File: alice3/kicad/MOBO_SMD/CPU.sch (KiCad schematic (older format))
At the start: 5 parts, among them U1 Z80CPU-SMD, U6 AS6C2008_TSOP

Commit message: Assign parts to footprints.
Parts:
- U1: footprint (none) -> Housings_QFP:LQFP-44_10x10mm_Pitch0.8mm
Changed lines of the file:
@@
 $EndDescr
 $Comp
-L GND #PWR42
+L GND #PWR042
 U 1 1 568DE0B3
 P 3950 4600
-F 0 "#PWR42" H 3950 4350 50  0001 C CNN
+F 0 "#PWR042" H 3950 4350 50  0001 C CNN
 F 1 "GND" H 3950 4450 50  0000 C CNN
 F 2 "" H 3950 4600 50  0000 C CNN
@@
 /Z80_RESET
 $Comp
-L GND #PWR40
+L GND #PWR043
 U 1 1 568DF463
 P 2200 2600
-F 0 "#PWR40" H 2200 2350 50  0001 C CNN
+F 0 "#PWR043" H 2200 2350 50  0001 C CNN
 F 1 "GND" H 2200 2450 50  0000 C CNN
 F 2 "" H 2200 2600 50  0000 C CNN
@@
 	3300 3100 3400 3100
 $Comp
-L GND #PWR44
+L GND #PWR044
 U 1 1 56A06CAB
 P 4450 1200
-F 0 "#PWR44" H 4450 950 50  0001 C CNN
+F 0 "#PWR044" H 4450 950 50  0001 C CNN
 F 1 "GND" H 4450 1050 50  0000 C CNN
 F 2 "" H 4450 1200 50  0000 C CNN
@@
 $EndComp
 $Comp
-L GND #PWR48
+L GND #PWR045
 U 1 1 56A06F73
 P 8100 1500
-F 0 "#PWR48" H 8100 1250 50  0001 C CNN
+F 0 "#PWR045" H 8100 1250 50  0001 C CNN
 F 1 "GND" H 8100 1350 50  0000 C CNN
 F 2 "" H 8100 1500 50  0000 C CNN
@@
 $EndComp
 $Comp
-L +3V3 #PWR43
+L +3V3 #PWR046
 U 1 1 56A5493F
 P 4100 800
-F 0 "#PWR43" H 4100 650 50  0001 C CNN
+F 0 "#PWR046" H 4100 650 50  0001 C CNN
 F 1 "+3V3" H 4100 940 50  0000 C CNN
 F 2 "" H 4100 800 60  0000 C CNN
@@
 $EndComp
 $Comp
-L +3V3 #PWR41
+L +3V3 #PWR047
 U 1 1 56A55184
 P 3200 2350
-F 0 "#PWR41" H 3200 2200 50  0001 C CNN
+F 0 "#PWR047" H 3200 2200 50  0001 C CNN
 F 1 "+3V3" H 3200 2490 50  0000 C CNN
 F 2 "" H 3200 2350 60  0000 C CNN
@@
 D0
 $Comp
-L GND #PWR47
+L GND #PWR048
 U 1 1 56CACCBC
 P 7650 4375
-F 0 "#PWR47" H 7650 4125 50  0001 C CNN
+F 0 "#PWR048" H 7650 4125 50  0001 C CNN
 F 1 "GND" H 7650 4225 50  0000 C CNN
 F 2 "" H 7650 4375 50  0000 C CNN
@@
 $EndComp
 $Comp
-L +3V3 #PWR46
+L +3V3 #PWR049
 U 1 1 56CACE05
 P 7650 900
-F 0 "#PWR46" H 7650 750 50  0001 C CNN
+F 0 "#PWR049" H 7650 750 50  0001 C CNN
 F 1 "+3V3" H 7650 1040 50  0000 C CNN
 F 2 "" H 7650 900 60  0000 C CNN
@@
 $EndComp
 $Comp
-L GND #PWR45
+L GND #PWR050
 U 1 1 56CACF44
 P 6400 3875
-F 0 "#PWR45" H 6400 3625 50  0001 C CNN
+F 0 "#PWR050" H 6400 3625 50  0001 C CNN
 F 1 "GND" H 6400 3725 50  0000 C CNN
 F 2 "" H 6400 3875 50  0000 C CNN
@@
 F 0 "U1" H 3550 4400 50  0000 L CNN
 F 1 "Z80CPU-SMD" H 4200 4400 50  0000 L CNN
-F 2 "" H 4100 3400 50  0000 C CNN
+F 2 "Housings_QFP:LQFP-44_10x10mm_Pitch0.8mm" H 4100 3400 50  0001 C CNN
 F 3 "" H 4100 3400 50  0000 C CNN
 	1    4100 3000
@@
 F 0 "U6" H 7425 4125 50  0000 C CNN
 F 1 "AS6C2008_TSOP" H 8025 1600 50  0000 C CNN
-F 2 "" H 7750 2925 50  0000 C CNN
+F 2 "" H 7750 2925 50  0001 C CNN
 F 3 "" H 7750 2925 50  0000 C CNN
 	1    7750 2925

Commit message: Fix some footprint assignments.
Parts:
- U6: footprint (none) -> SMD_Packages:TSOP32SP
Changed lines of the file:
@@
 $EndDescr
 $Comp
-L GND #PWR042
+L GND #PWR043
 U 1 1 568DE0B3
 P 3950 4600
-F 0 "#PWR042" H 3950 4350 50  0001 C CNN
+F 0 "#PWR043" H 3950 4350 50  0001 C CNN
 F 1 "GND" H 3950 4450 50  0000 C CNN
 F 2 "" H 3950 4600 50  0000 C CNN
@@
 /Z80_RESET
 $Comp
-L GND #PWR043
+L GND #PWR044
 U 1 1 568DF463
 P 2200 2600
-F 0 "#PWR043" H 2200 2350 50  0001 C CNN
+F 0 "#PWR044" H 2200 2350 50  0001 C CNN
 F 1 "GND" H 2200 2450 50  0000 C CNN
 F 2 "" H 2200 2600 50  0000 C CNN
@@
 	3300 3100 3400 3100
 $Comp
-L GND #PWR044
+L GND #PWR045
 U 1 1 56A06CAB
 P 4450 1200
-F 0 "#PWR044" H 4450 950 50  0001 C CNN
+F 0 "#PWR045" H 4450 950 50  0001 C CNN
 F 1 "GND" H 4450 1050 50  0000 C CNN
 F 2 "" H 4450 1200 50  0000 C CNN
@@
 $EndComp
 $Comp
-L GND #PWR045
+L GND #PWR046
 U 1 1 56A06F73
 P 8100 1500
-F 0 "#PWR045" H 8100 1250 50  0001 C CNN
+F 0 "#PWR046" H 8100 1250 50  0001 C CNN
 F 1 "GND" H 8100 1350 50  0000 C CNN
 F 2 "" H 8100 1500 50  0000 C CNN
@@
 $EndComp
 $Comp
-L +3V3 #PWR046
+L +3V3 #PWR047
 U 1 1 56A5493F
 P 4100 800
-F 0 "#PWR046" H 4100 650 50  0001 C CNN
+F 0 "#PWR047" H 4100 650 50  0001 C CNN
 F 1 "+3V3" H 4100 940 50  0000 C CNN
 F 2 "" H 4100 800 60  0000 C CNN
@@
 $EndComp
 $Comp
-L +3V3 #PWR047
+L +3V3 #PWR048
 U 1 1 56A55184
 P 3200 2350
-F 0 "#PWR047" H 3200 2200 50  0001 C CNN
+F 0 "#PWR048" H 3200 2200 50  0001 C CNN
 F 1 "+3V3" H 3200 2490 50  0000 C CNN
 F 2 "" H 3200 2350 60  0000 C CNN
@@
 D0
 $Comp
-L GND #PWR048
+L GND #PWR049
 U 1 1 56CACCBC
 P 7650 4375
-F 0 "#PWR048" H 7650 4125 50  0001 C CNN
+F 0 "#PWR049" H 7650 4125 50  0001 C CNN
 F 1 "GND" H 7650 4225 50  0000 C CNN
 F 2 "" H 7650 4375 50  0000 C CNN
@@
 $EndComp
 $Comp
-L +3V3 #PWR049
+L +3V3 #PWR050
 U 1 1 56CACE05
 P 7650 900
-F 0 "#PWR049" H 7650 750 50  0001 C CNN
+F 0 "#PWR050" H 7650 750 50  0001 C CNN
 F 1 "+3V3" H 7650 1040 50  0000 C CNN
 F 2 "" H 7650 900 60  0000 C CNN
@@
 $EndComp
 $Comp
-L GND #PWR050
+L GND #PWR051
 U 1 1 56CACF44
 P 6400 3875
-F 0 "#PWR050" H 6400 3625 50  0001 C CNN
+F 0 "#PWR051" H 6400 3625 50  0001 C CNN
 F 1 "GND" H 6400 3725 50  0000 C CNN
 F 2 "" H 6400 3875 50  0000 C CNN
@@
 F 0 "U6" H 7425 4125 50  0000 C CNN
 F 1 "AS6C2008_TSOP" H 8025 1600 50  0000 C CNN
-F 2 "" H 7750 2925 50  0001 C CNN
+F 2 "SMD_Packages:TSOP32SP" H 7750 2925 50  0001 C CNN
 F 3 "" H 7750 2925 50  0000 C CNN
 	1    7750 2925

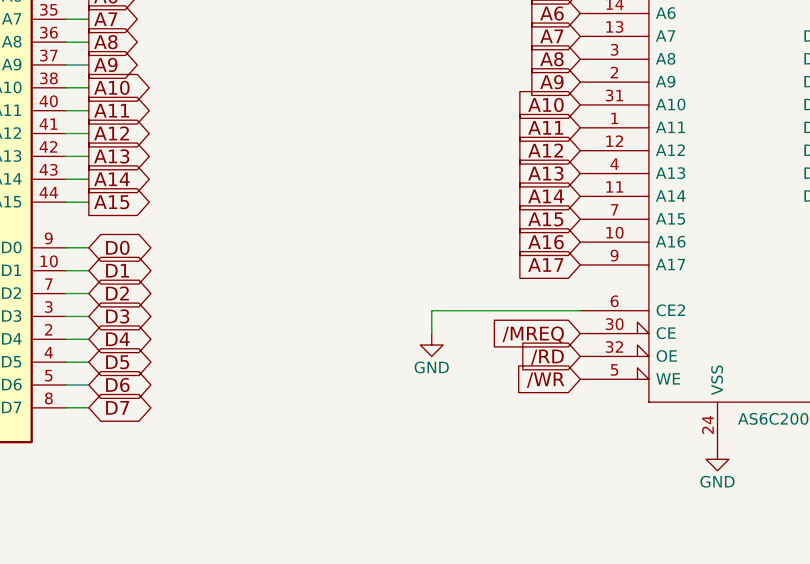
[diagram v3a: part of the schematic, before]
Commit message: Point out bug in Alice 3 schematic.
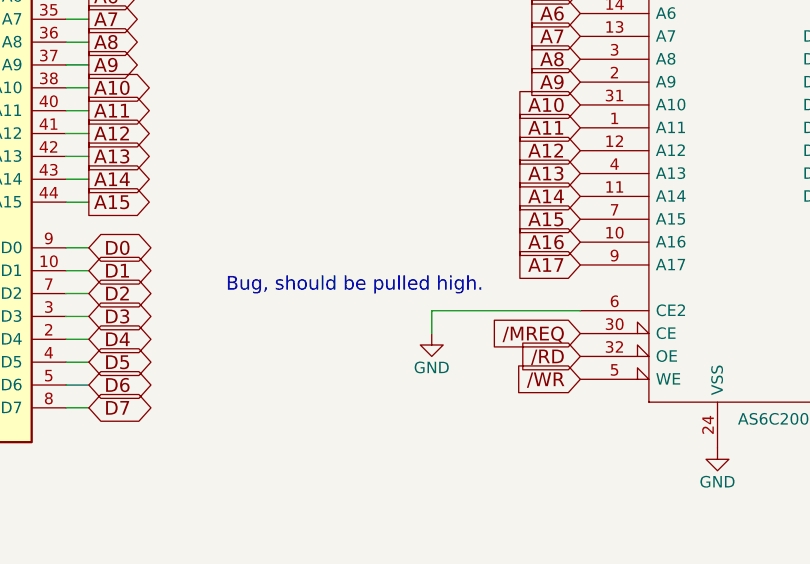
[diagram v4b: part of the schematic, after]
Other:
- note added: "Bug, should be pulled high."
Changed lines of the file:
@@
 Wire Wire Line
 	8100 1500 8100 1450
+Text Notes 5500 3700 0    60   ~ 0
+Bug, should be pulled high.
 $EndSCHEMATC

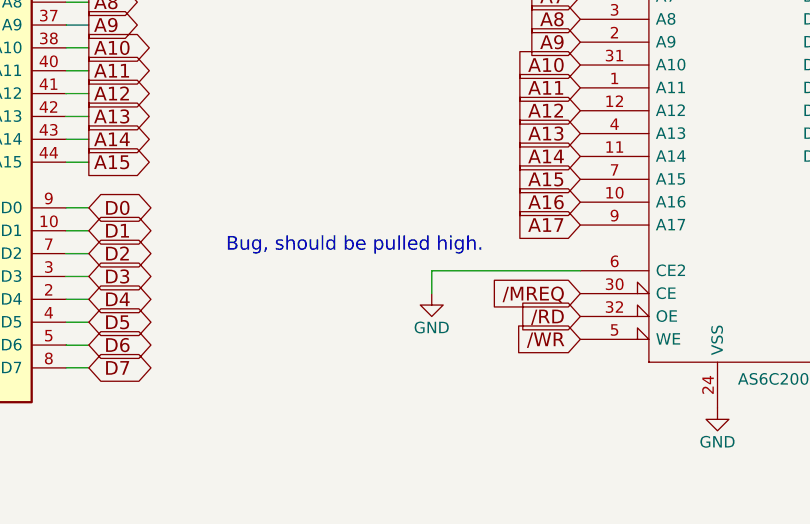
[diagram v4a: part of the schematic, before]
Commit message: make CE2 high
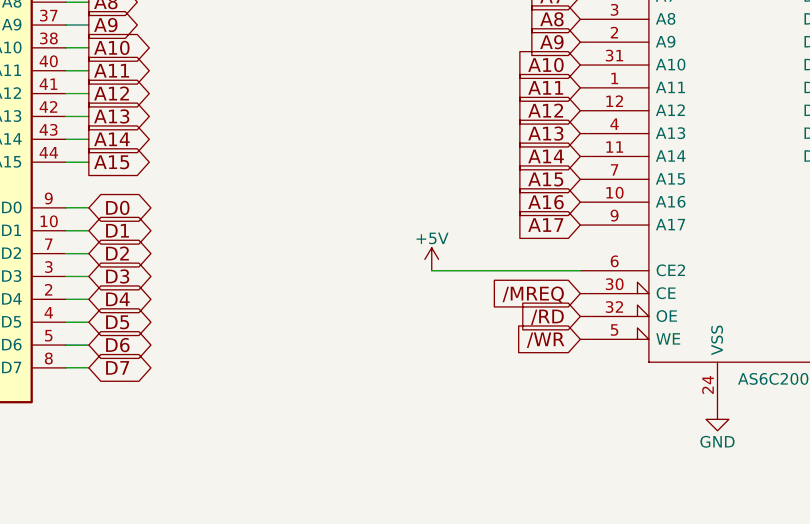
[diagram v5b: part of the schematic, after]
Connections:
- net GND: no longer U6.6 (CE2)
- new net +5V: U6.6 (CE2)
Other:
- note removed: "Bug, should be pulled high."
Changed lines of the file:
@@
-$EndComp
-$Comp
-L GND #PWR050
-U 1 1 56CACF44
-P 6400 3875
-F 0 "#PWR050" H 6400 3625 50  0001 C CNN
-F 1 "GND" H 6400 3725 50  0000 C CNN
-F 2 "" H 6400 3875 50  0000 C CNN
-F 3 "" H 6400 3875 50  0000 C CNN
-	1    6400 3875
-	1    0    0    -1
 $EndComp
 $Comp
@@
 Wire Wire Line
 	7050 3775 6400 3775
-Wire Wire Line
-	6400 3775 6400 3875
 Text GLabel 7050 3575 0    60   Input ~ 0
 A17
@@
 Wire Wire Line
 	8100 1500 8100 1450
-Text Notes 5500 3700 0    60   ~ 0
-Bug, should be pulled high.
+$Comp
+L +5V #PWR?
+U 1 1 59948058
+P 6400 3775
+F 0 "#PWR?" H 6400 3625 50  0001 C CNN
+F 1 "+5V" H 6400 3915 50  0000 C CNN
+F 2 "" H 6400 3775 50  0001 C CNN
+F 3 "" H 6400 3775 50  0001 C CNN
+	1    6400 3775
+	1    0    0    -1
+$EndComp
 $EndSCHEMATC

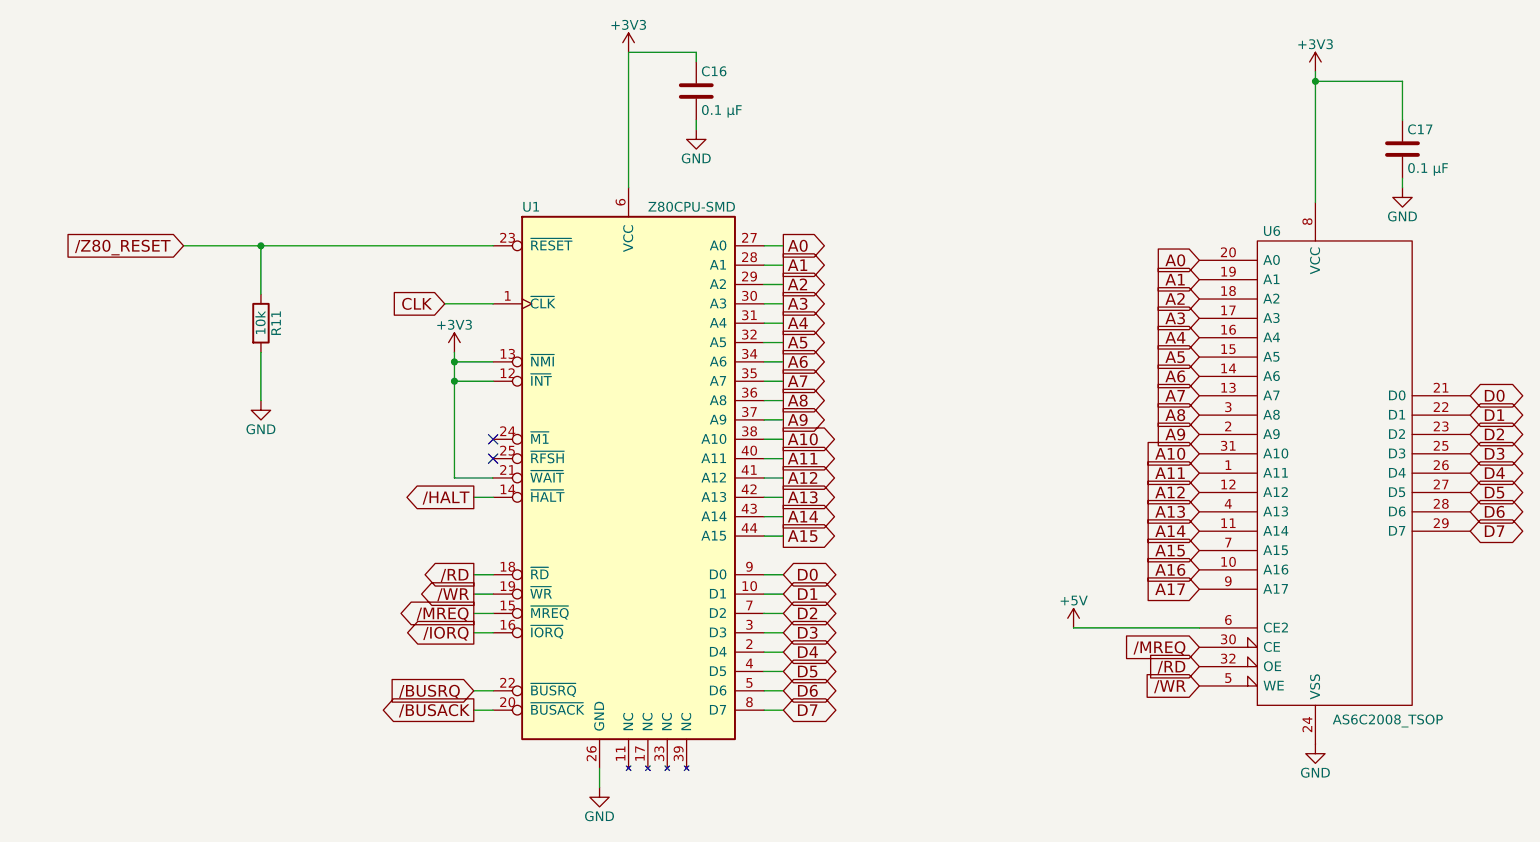
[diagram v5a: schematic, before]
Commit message: 1st set MOBO schematic fixes for 1st PCBWay spin
Various fixes for KiCAD messing up components

Button on BOOT0

No huge cap on power supply LED

Discard RAM

Route ARM to Z80 /WAIT and /RFSH

Use "~" for active-low lines (shown in schematic by line above them)
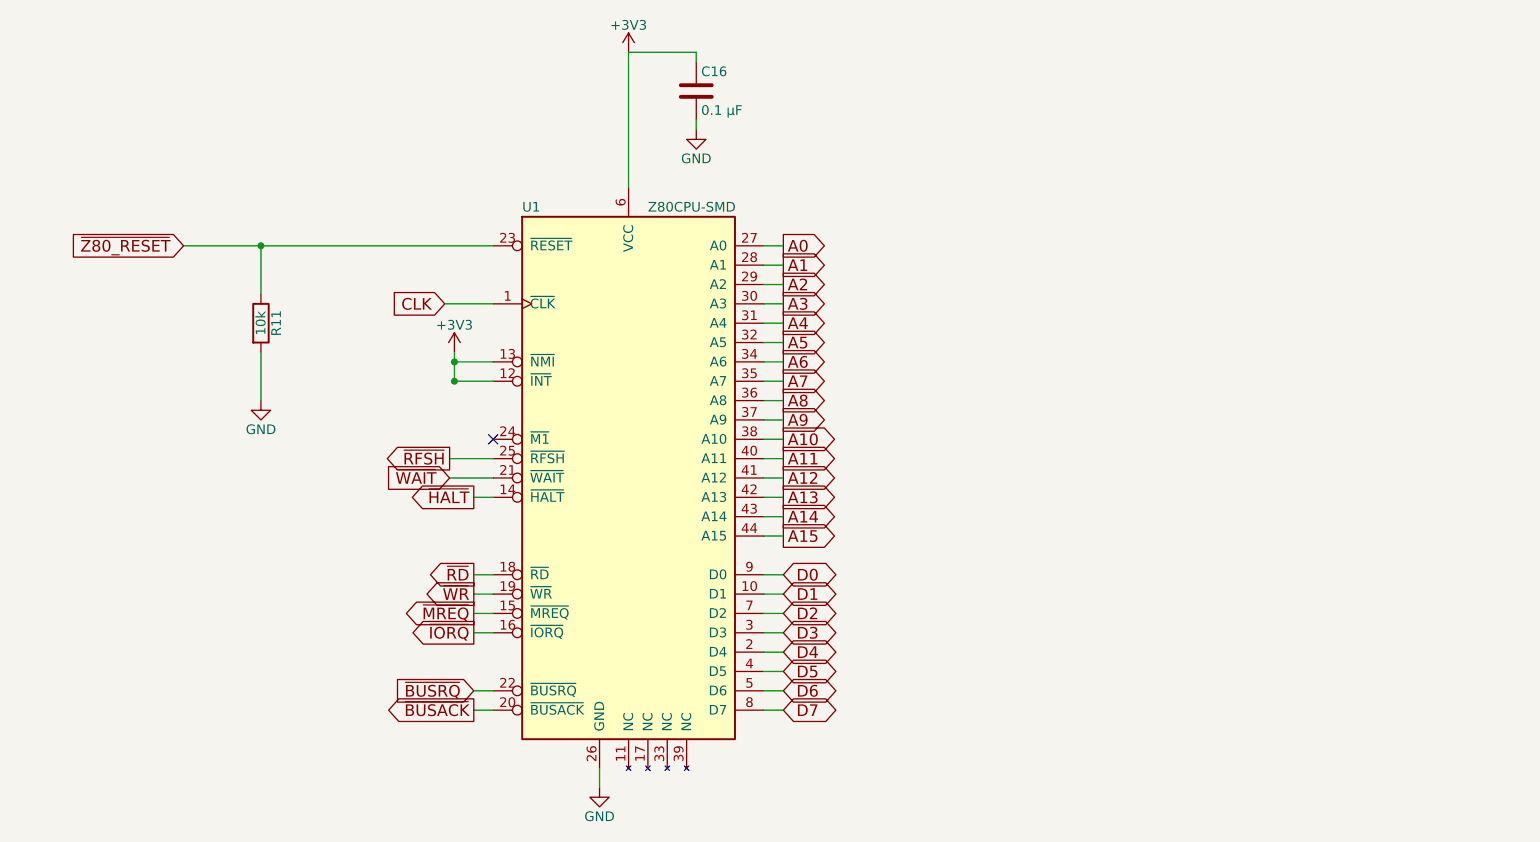
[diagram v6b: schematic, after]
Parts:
- removed C17: 0.1 µF, Capacitors_SMD:C_0805, symbol C
- removed U6: AS6C2008_TSOP, SMD_Packages:TSOP32SP, symbol AS6C2008_TSOP
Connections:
- net +3V3: no longer U1.21 (~WAIT~)
- net ~RFSH: now reaches U1.25 (~RFSH~)
- net /BUSACK renamed ~BUSACK
- net /BUSRQ renamed ~BUSRQ
- net /HALT renamed ~HALT
- net /IORQ renamed ~IORQ
- net /MREQ renamed ~MREQ
- net /RD renamed ~RD
- net /WR renamed ~WR
- net /Z80_RESET renamed ~Z80_RESET
- new net ~WAIT: U1.21 (~WAIT~)
- no-connect marks 2 -> 1
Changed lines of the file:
@@
 $EndDescr
 $Comp
-L GND #PWR042
+L GND #PWR037
 U 1 1 568DE0B3
 P 3950 4600
-F 0 "#PWR042" H 3950 4350 50  0001 C CNN
+F 0 "#PWR037" H 3950 4350 50  0001 C CNN
 F 1 "GND" H 3950 4450 50  0000 C CNN
 F 2 "" H 3950 4600 50  0000 C CNN
@@
 D0
 Wire Wire Line
-	3200 2350 3200 3000
-Wire Wire Line
 	3200 2400 3400 2400
 Connection ~ 3200 2400
 Text GLabel 3300 3500 0    60   Output ~ 0
-/RD
+~RD
 Text GLabel 3300 3600 0    60   Output ~ 0
-/WR
+~WR
 Text GLabel 3300 3700 0    60   Output ~ 0
-/MREQ
+~MREQ
 Text GLabel 3300 3800 0    60   Output ~ 0
-/IORQ
+~IORQ
 Wire Wire Line
 	3300 3500 3400 3500
@@
 Wire Wire Line
 	3300 3800 3400 3800
-NoConn ~ 3400 2900
-Wire Wire Line
-	3200 3000 3400 3000
 NoConn ~ 3400 2800
 Text GLabel 3300 4100 0    60   Input ~ 0
-/BUSRQ
+~BUSRQ
 Text GLabel 3300 4200 0    60   Output ~ 0
-/BUSACK
+~BUSACK
 Wire Wire Line
 	3300 4200 3400 4200
 Text GLabel 1800 1800 0    60   Input ~ 0
-/Z80_RESET
-$Comp
-L GND #PWR043
+~Z80_RESET
+$Comp
+L GND #PWR038
 U 1 1 568DF463
 P 2200 2600
-F 0 "#PWR043" H 2200 2350 50  0001 C CNN
+F 0 "#PWR038" H 2200 2350 50  0001 C CNN
 F 1 "GND" H 2200 2450 50  0000 C CNN
 F 2 "" H 2200 2600 50  0000 C CNN
@@
 Connection ~ 3200 2500
 Text GLabel 3300 3100 0    60   Output ~ 0
-/HALT
+~HALT
 Wire Wire Line
 	3300 3100 3400 3100
 $Comp
-L GND #PWR044
+L GND #PWR039
 U 1 1 56A06CAB
 P 4450 1200
-F 0 "#PWR044" H 4450 950 50  0001 C CNN
+F 0 "#PWR039" H 4450 950 50  0001 C CNN
 F 1 "GND" H 4450 1050 50  0000 C CNN
 F 2 "" H 4450 1200 50  0000 C CNN
@@
 	4450 800  4450 850
 $Comp
-L C C17
-U 1 1 56A06F35
-P 8100 1300
-F 0 "C17" H 8125 1400 50  0000 L CNN
-F 1 "0.1 µF" H 8125 1200 50  0000 L CNN
-F 2 "Capacitors_SMD:C_0805" H 8138 1150 50  0001 C CNN
-F 3 "" H 8100 1300 50  0000 C CNN
-	1    8100 1300
-	1    0    0    -1
-$EndComp
-$Comp
-L GND #PWR045
-U 1 1 56A06F73
-P 8100 1500
-F 0 "#PWR045" H 8100 1250 50  0001 C CNN
-F 1 "GND" H 8100 1350 50  0000 C CNN
-F 2 "" H 8100 1500 50  0000 C CNN
-F 3 "" H 8100 1500 50  0000 C CNN
-	1    8100 1500
-	1    0    0    -1
-$EndComp
-$Comp
-L +3V3 #PWR046
+L +3V3 #PWR040
 U 1 1 56A5493F
 P 4100 800
-F 0 "#PWR046" H 4100 650 50  0001 C CNN
+F 0 "#PWR040" H 4100 650 50  0001 C CNN
 F 1 "+3V3" H 4100 940 50  0000 C CNN
 F 2 "" H 4100 800 60  0000 C CNN
@@
 $EndComp
 $Comp
-L +3V3 #PWR047
+L +3V3 #PWR041
 U 1 1 56A55184
 P 3200 2350
-F 0 "#PWR047" H 3200 2200 50  0001 C CNN
+F 0 "#PWR041" H 3200 2200 50  0001 C CNN
 F 1 "+3V3" H 3200 2490 50  0000 C CNN
 F 2 "" H 3200 2350 60  0000 C CNN
 F 3 "" H 3200 2350 60  0000 C CNN
 	1    3200 2350
-	1    0    0    -1
-$EndComp
-Text GLabel 7050 3375 0    60   Input ~ 0
-A15
-Text GLabel 7050 3275 0    60   Input ~ 0
-A14
-Text GLabel 7050 3175 0    60   Input ~ 0
-A13
-Text GLabel 7050 3075 0    60   Input ~ 0
-A12
-Text GLabel 7050 2975 0    60   Input ~ 0
-A11
-Text GLabel 7050 2875 0    60   Input ~ 0
-A10
-Text GLabel 7050 2775 0    60   Input ~ 0
-A9
-Text GLabel 7050 2675 0    60   Input ~ 0
-A8
-Text GLabel 7050 2575 0    60   Input ~ 0
-A7
-Text GLabel 7050 2475 0    60   Input ~ 0
-A6
-Text GLabel 7050 2375 0    60   Input ~ 0
-A5
-Text GLabel 7050 2275 0    60   Input ~ 0
-A4
-Text GLabel 7050 2175 0    60   Input ~ 0
-A3
-Text GLabel 7050 2075 0    60   Input ~ 0
-A2
-Text GLabel 7050 1975 0    60   Input ~ 0
-A1
-Text GLabel 7050 1875 0    60   Input ~ 0
-A0
-Text GLabel 7050 3475 0    60   Input ~ 0
-A16
-Text GLabel 7050 3875 0    60   Input ~ 0
-/MREQ
-Text GLabel 7050 3975 0    60   Input ~ 0
-/RD
-Text GLabel 7050 4075 0    60   Input ~ 0
-/WR
-Text GLabel 8450 3275 2    60   BiDi ~ 0
-D7
-Text GLabel 8450 3175 2    60   BiDi ~ 0
-D6
-Text GLabel 8450 3075 2    60   BiDi ~ 0
-D5
-Text GLabel 8450 2975 2    60   BiDi ~ 0
-D4
-Text GLabel 8450 2875 2    60   BiDi ~ 0
-D3
-Text GLabel 8450 2775 2    60   BiDi ~ 0
-D2
-Text GLabel 8450 2675 2    60   BiDi ~ 0
-D1
-Text GLabel 8450 2575 2    60   BiDi ~ 0
-D0
-$Comp
-L GND #PWR048
-U 1 1 56CACCBC
-P 7650 4375
-F 0 "#PWR048" H 7650 4125 50  0001 C CNN
-F 1 "GND" H 7650 4225 50  0000 C CNN
-F 2 "" H 7650 4375 50  0000 C CNN
-F 3 "" H 7650 4375 50  0000 C CNN
-	1    7650 4375
-	1    0    0    -1
-$EndComp
-$Comp
-L +3V3 #PWR049
-U 1 1 56CACE05
-P 7650 900
-F 0 "#PWR049" H 7650 750 50  0001 C CNN
-F 1 "+3V3" H 7650 1040 50  0000 C CNN
-F 2 "" H 7650 900 60  0000 C CNN
-F 3 "" H 7650 900 60  0000 C CNN
-	1    7650 900
 	1    0    0    -1
 $EndComp
@@
 	3950 4600 3950 4500
 Wire Wire Line
-	7050 3775 6400 3775
-Text GLabel 7050 3575 0    60   Input ~ 0
-A17
-Wire Wire Line
 	3300 4100 3400 4100
-$Comp
-L AS6C2008_TSOP U6
-U 1 1 56D3979F
-P 7750 2925
-F 0 "U6" H 7425 4125 50  0000 C CNN
-F 1 "AS6C2008_TSOP" H 8025 1600 50  0000 C CNN
-F 2 "SMD_Packages:TSOP32SP" H 7750 2925 50  0001 C CNN
-F 3 "" H 7750 2925 50  0000 C CNN
-	1    7750 2925
-	1    0    0    -1
-$EndComp
-Wire Wire Line
-	7650 1575 7650 900
-Wire Wire Line
-	8100 1150 8100 950
-Wire Wire Line
-	8100 950  7650 950
-Connection ~ 7650 950
-Wire Wire Line
-	8100 1500 8100 1450
-$Comp
-L +5V #PWR?
-U 1 1 59948058
-P 6400 3775
-F 0 "#PWR?" H 6400 3625 50  0001 C CNN
-F 1 "+5V" H 6400 3915 50  0000 C CNN
-F 2 "" H 6400 3775 50  0001 C CNN
-F 3 "" H 6400 3775 50  0001 C CNN
-	1    6400 3775
-	1    0    0    -1
-$EndComp
+Wire Wire Line
+	3200 2500 3200 2350
+Text GLabel 3175 3000 0    60   Input ~ 0
+~WAIT
+Text GLabel 3175 2900 0    60   Output ~ 0
+~RFSH
+Wire Wire Line
+	3175 3000 3400 3000
+Wire Wire Line
+	3400 2900 3175 2900
 $EndSCHEMATC

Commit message: fix inductor, fix HOME
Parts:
- U1: Distributor (none) -> Digikey; Distributor PN (none) -> 269-4575-ND; Manufacturer (none) -> Zilog; PN (none) -> Z84C0020AEG
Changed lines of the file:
@@
 LIBS:propeller_p8x32a-q44
 LIBS:as6c2008_tsop
+LIBS:conn-fci
 LIBS:MOBO_SMD-cache
 EELAYER 25 0
@@
 F 2 "Housings_QFP:LQFP-44_10x10mm_Pitch0.8mm" H 4100 3400 50  0001 C CNN
 F 3 "" H 4100 3400 50  0000 C CNN
+F 4 "Zilog" H 975 3575 60  0001 C CNN "Manufacturer"
+F 5 "Z84C0020AEG" H 975 3575 60  0001 C CNN "PN"
+F 6 "Digikey" H 975 3575 60  0001 C CNN "Distributor"
+F 7 "269-4575-ND" H 975 3575 60  0001 C CNN "Distributor PN"
 	1    4100 3000
 	1    0    0    -1
